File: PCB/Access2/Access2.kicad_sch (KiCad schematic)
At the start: 67 parts, among them J1 USB-C, J2 RFID, J3 INPUTS, J4 Shelly, J5 POWER, J6 DOOR, Q1 NX7002AK, SW1 ESE13V01D, U1 ESP32-PICO-MINI-02, U2 FT231XQ, U3 G3VM-41GR8, U4 LMR16006XDDCR, U5 LMR16006XDDCR, U6 AA, U7 QR

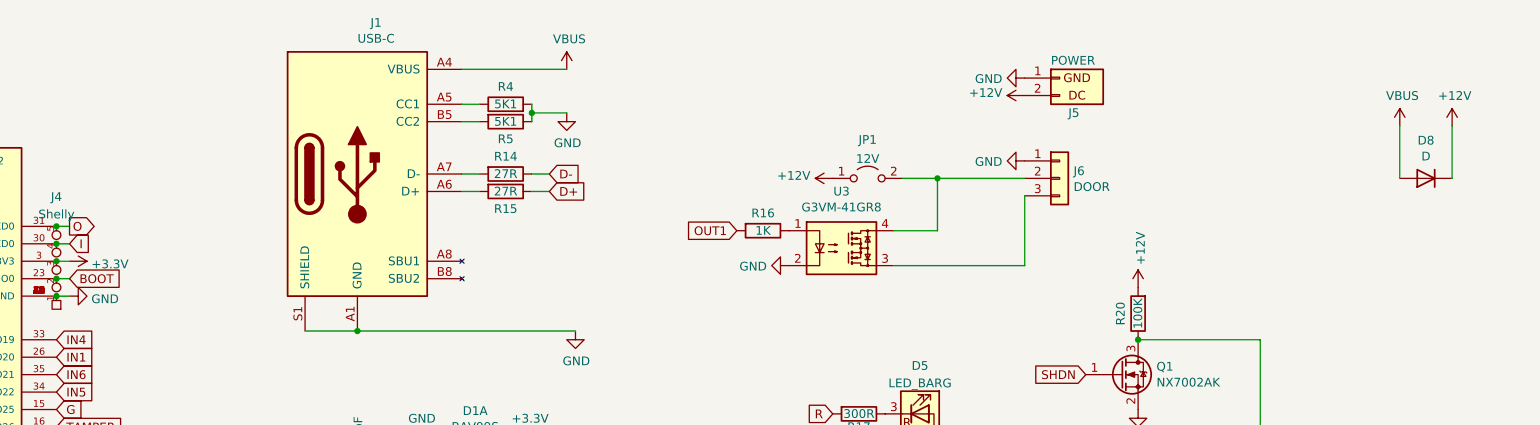
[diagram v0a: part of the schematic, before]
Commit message: Reverse polarity protection and additional capacitors for less clean supplies.
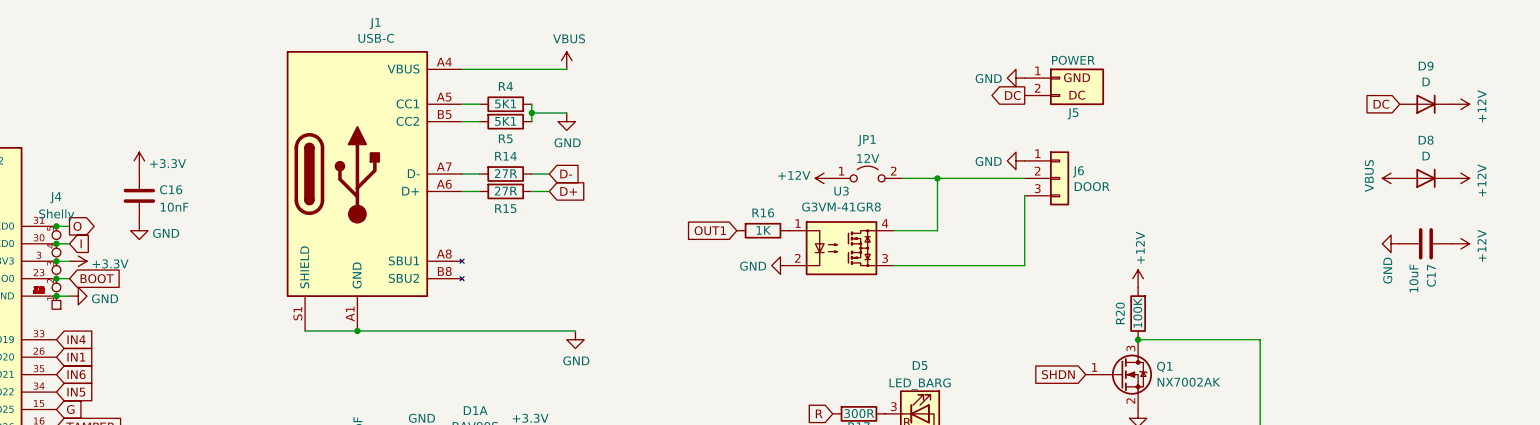
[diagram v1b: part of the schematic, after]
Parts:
- added C16: 10nF, RevK:C_0603, symbol Device:C
- added C17: 10uF, RevK:C_0603, symbol Device:C
- added D9: D, RevK:D_1206, symbol Device:D
- JP1: footprint Connector_PinHeader_1.27mm:PinHeader_1x02_P1.27mm_Vertical -> Jumper:SolderJumper-2_P1.3mm_Open_RoundedPad1.0x1.5mm; now left out of the parts list
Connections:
- net +12V: now also C17.1, D9.1 (K); no longer J5.2 (DC)
- net +3V3: now also C16.1
- net GND: now also C16.2, C17.2
- new net DC: D9.2 (A), J5.2 (DC)

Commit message: Position
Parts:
- C17: footprint RevK:C_0603 -> RevK:C_0805
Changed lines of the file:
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@@
       (effects (font (size 1.27 1.27)) (justify left))
     )
-    (property "Footprint" "RevK:C_0603" (id 2) (at 256.54 47.9552 0)
+    (property "Footprint" "RevK:C_0805" (id 2) (at 256.54 47.9552 0)
       (effects (font (size 1.27 1.27)) hide)
     )
@@
     )
     (path "/d8589cdf-5b78-401b-9664-7e16b1063c72"
-      (reference "C17") (unit 1) (value "10uF") (footprint "RevK:C_0603")
+      (reference "C17") (unit 1) (value "10uF") (footprint "RevK:C_0805")
     )
     (path "/00000000-0000-0000-0000-00006099fc70"

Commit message: Slight tidy
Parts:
- C10, C11, C13, C14: footprint RevK:C_0805_ -> RevK:Hidden
- C12, C9: footprint RevK:C_0603_ -> RevK:Hidden
- D6, D7: footprint RevK:D_1206_ -> RevK:Hidden
- L1, L2: footprint RevK:L_4x4_ -> RevK:Hidden
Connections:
- net BOOT: now also J4.4 (Rx); no longer J4.2 (0)
- net GND: now also J4.5 (Tx); no longer J4.1 (GND)
- net I: now also J4.2 (0); no longer J4.4 (Rx)
- net O: now also J4.1 (GND); no longer J4.5 (Tx)
- net +3V3 renamed +3.3V
- net IN1 renamed IO1
- net IN2 renamed IO2
- net IN3 renamed IO3
- net IN4 renamed IO4
- net IN5 renamed IO5
- net IN6 renamed IO6
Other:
- moved on the sheet: J4

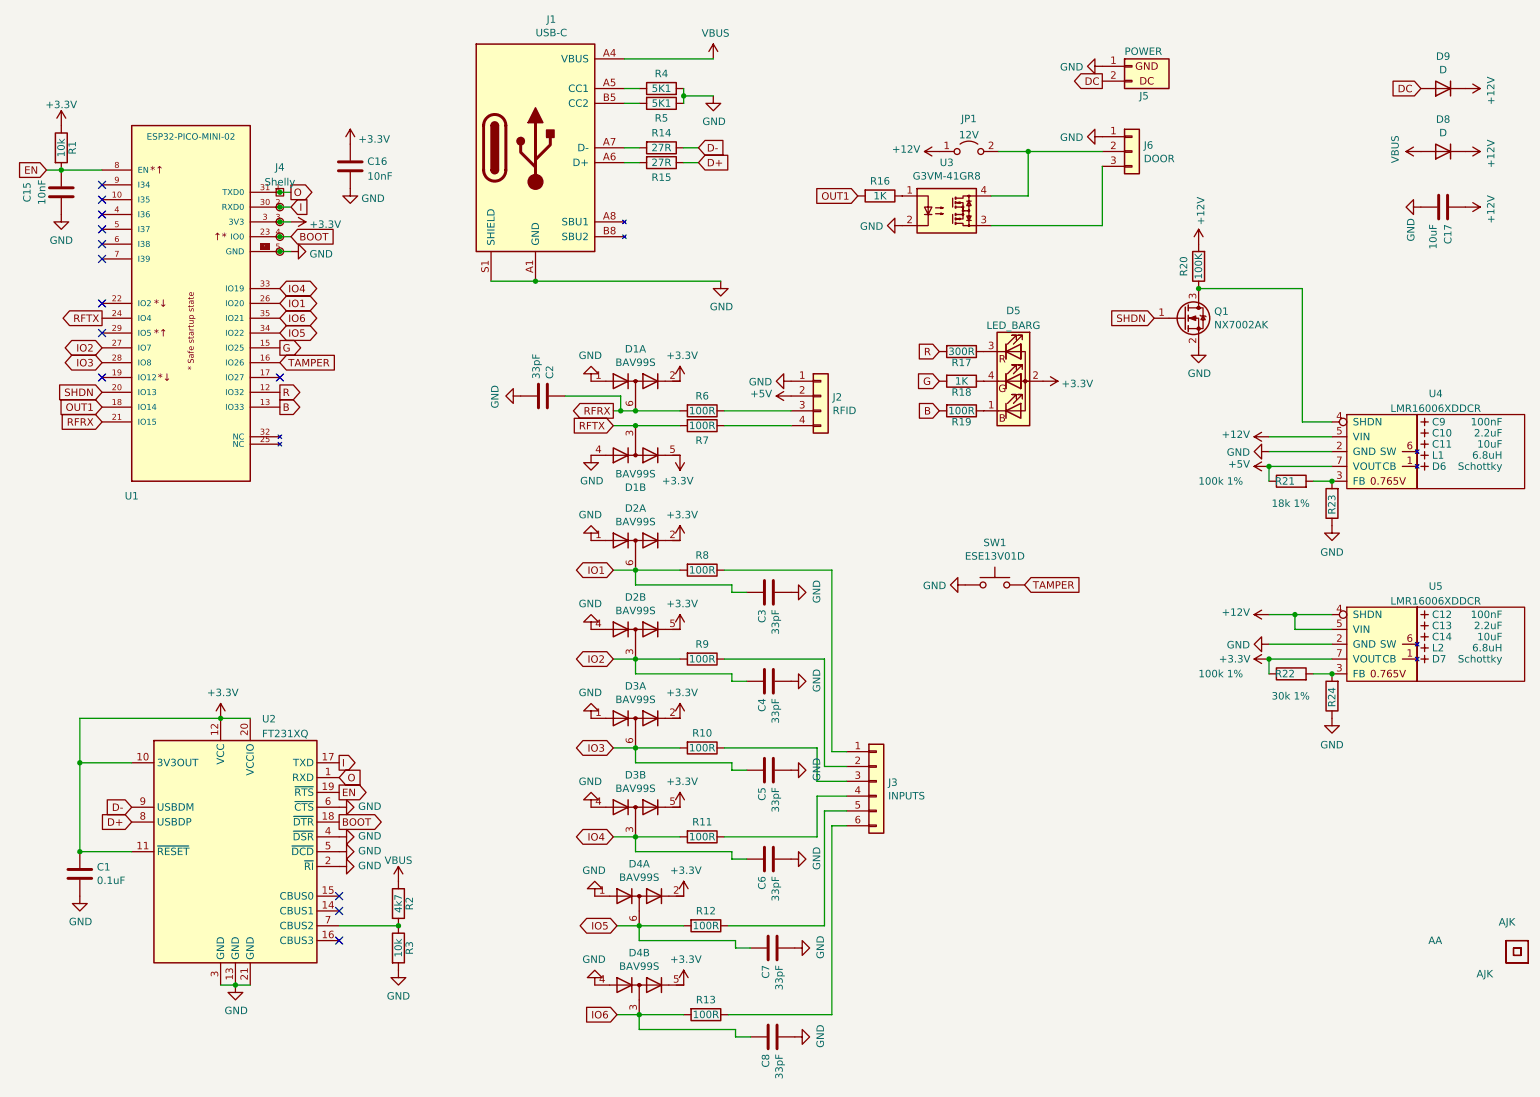
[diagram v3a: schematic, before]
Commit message: Added FET on NFC Rx
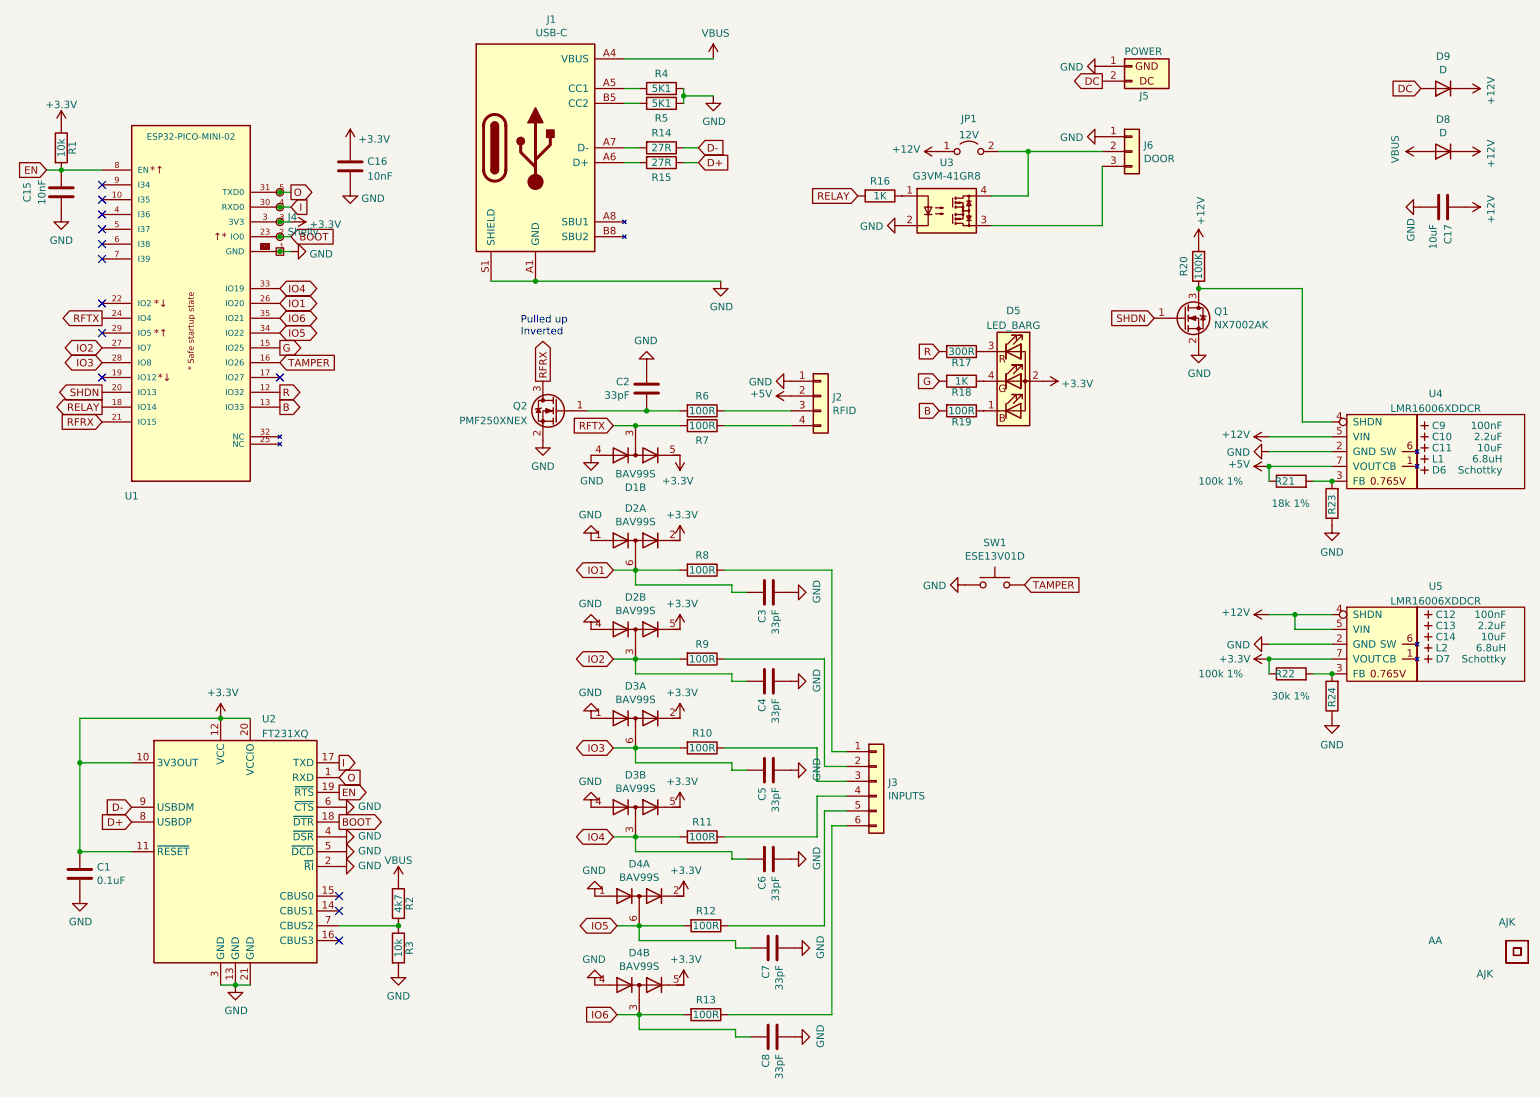
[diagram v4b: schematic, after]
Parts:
- removed unit 1 of D1
- added Q2: PMF250XNEX, RevK:SOT-323_SC-70, symbol RevK:NX7002AK
- C10, C11, C13, C14: footprint RevK:Hidden -> RevK:C_0805_
- C12, C9: footprint RevK:Hidden -> RevK:C_0603_
- D6, D7: footprint RevK:Hidden -> RevK:D_1206_; JLCPCB Rotation Offset (none) -> 180
- L1, L2: footprint RevK:Hidden -> RevK:L_4x4_
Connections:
- net BOOT: now also J4.2 (0); no longer J4.4 (Rx)
- net GND: now also C2.1, J4.1 (GND), Q2.2 (S); no longer C2.2, J4.5 (Tx)
- net I: now also J4.4 (Rx); no longer J4.2 (0)
- net O: now also J4.5 (Tx); no longer J4.1 (GND)
- net RFRX: now also Q2.3 (D); no longer C2.1, R6.2
- net OUT1 renamed RELAY
- new net: C2.2, Q2.1 (G), R6.2
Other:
- note added: "Pulled up Inverted"
- moved on the sheet: C2, J4

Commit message: New connectors
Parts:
- J2: footprint RevK:Molex_MiniSPOX_H4RA -> RevK:PTSM-HH-4-RA
- J3: footprint RevK:Molex_MiniSPOX_H6RA -> RevK:PTSM-HH-6-RA
- J5: footprint RevK:Molex_MiniSPOX_H2RA -> RevK:PTSM-HH1-2-RA
- J6: footprint RevK:Molex_MiniSPOX_H3RA -> RevK:PTSM-HH1-3-RA
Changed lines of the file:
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@@
       (effects (font (size 1.27 1.27)) (justify left))
     )
-    (property "Footprint" "RevK:Molex_MiniSPOX_H4RA" (id 2) (at 153.67 79.375 0)
+    (property "Footprint" "RevK:PTSM-HH-4-RA" (id 2) (at 153.67 79.375 0)
       (effects (font (size 1.27 1.27)) hide)
     )
@@
       (effects (font (size 1.27 1.27)) (justify left))
     )
-    (property "Footprint" "RevK:Molex_MiniSPOX_H2RA" (id 2) (at 207.01 22.86 0)
+    (property "Footprint" "RevK:PTSM-HH1-2-RA" (id 2) (at 207.01 22.86 0)
       (effects (font (size 1.27 1.27)) hide)
     )
@@
       (effects (font (size 1.27 1.27)) (justify left))
     )
-    (property "Footprint" "RevK:Molex_MiniSPOX_H3RA" (id 2) (at 207.01 37.465 0)
+    (property "Footprint" "RevK:PTSM-HH1-3-RA" (id 2) (at 207.01 37.465 0)
       (effects (font (size 1.27 1.27)) hide)
     )
@@
       (effects (font (size 1.27 1.27)) (justify left))
     )
-    (property "Footprint" "RevK:Molex_MiniSPOX_H6RA" (id 2) (at 163.195 145.415 0)
+    (property "Footprint" "RevK:PTSM-HH-6-RA" (id 2) (at 163.195 145.415 0)
       (effects (font (size 1.27 1.27)) hide)
     )
@@
     )
     (path "/00000000-0000-0000-0000-000060739fa0"
-      (reference "J2") (unit 1) (value "RFID") (footprint "RevK:Molex_MiniSPOX_H4RA")
+      (reference "J2") (unit 1) (value "RFID") (footprint "RevK:PTSM-HH-4-RA")
     )
     (path "/00000000-0000-0000-0000-0000608cf414"
-      (reference "J3") (unit 1) (value "INPUTS") (footprint "RevK:Molex_MiniSPOX_H6RA")
+      (reference "J3") (unit 1) (value "INPUTS") (footprint "RevK:PTSM-HH-6-RA")
     )
     (path "/054d3fd2-4931-4b9d-baac-1a45d3fc9bae"
@@
     )
     (path "/00000000-0000-0000-0000-00006074263f"
-      (reference "J5") (unit 1) (value "POWER") (footprint "RevK:Molex_MiniSPOX_H2RA")
+      (reference "J5") (unit 1) (value "POWER") (footprint "RevK:PTSM-HH1-2-RA")
     )
     (path "/00000000-0000-0000-0000-0000608cb396"
-      (reference "J6") (unit 1) (value "DOOR") (footprint "RevK:Molex_MiniSPOX_H3RA")
+      (reference "J6") (unit 1) (value "DOOR") (footprint "RevK:PTSM-HH1-3-RA")
     )
     (path "/b9e3b3a7-ba8d-4414-9892-926f9909a922"
